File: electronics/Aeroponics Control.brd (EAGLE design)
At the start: 61.9 x 71.1 mm, 27 parts, among them IC1 7407N, K1 SRM-1C-SL-5VDC, Q1 FQP30N06L, Q2 FQP30N06L, Q6 FDU3N40TU

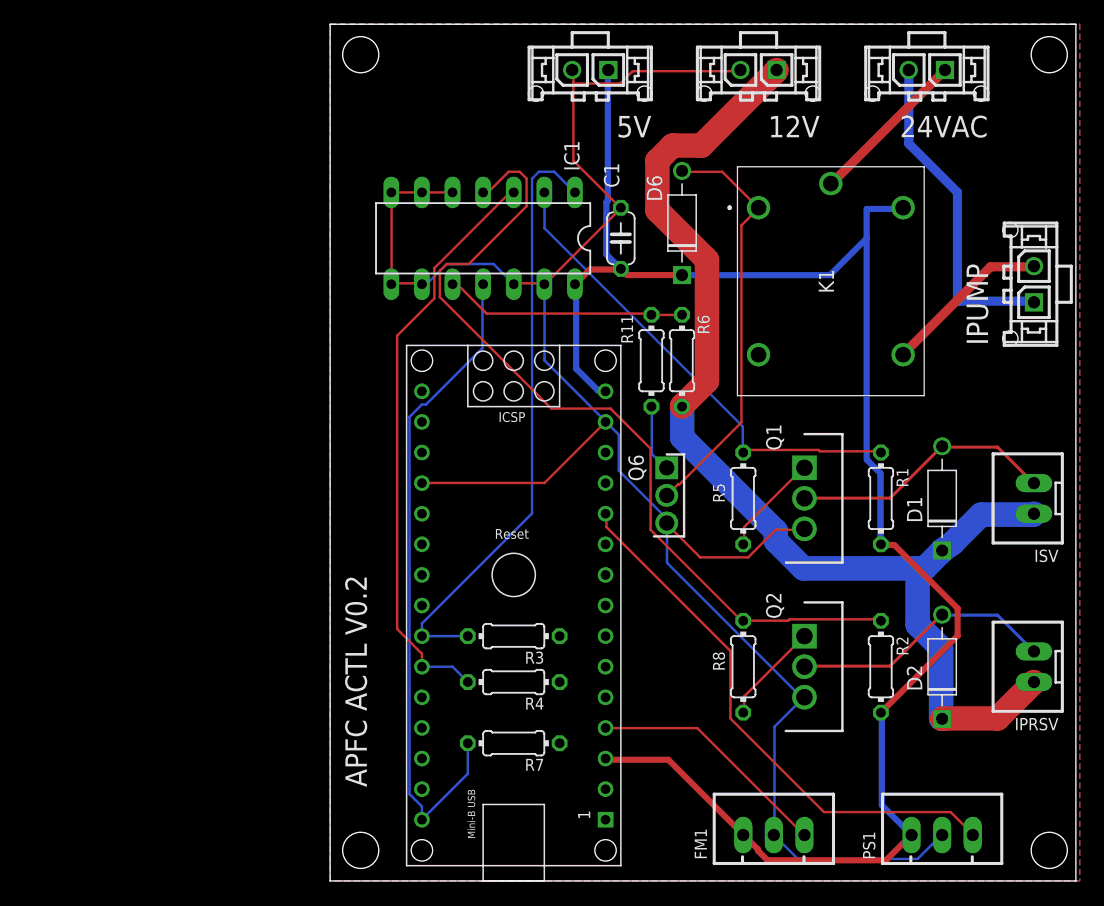
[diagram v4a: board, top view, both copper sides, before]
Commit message: Fixed FMS1 pin assignment on Nano. Incorpated fixed Relay library component.
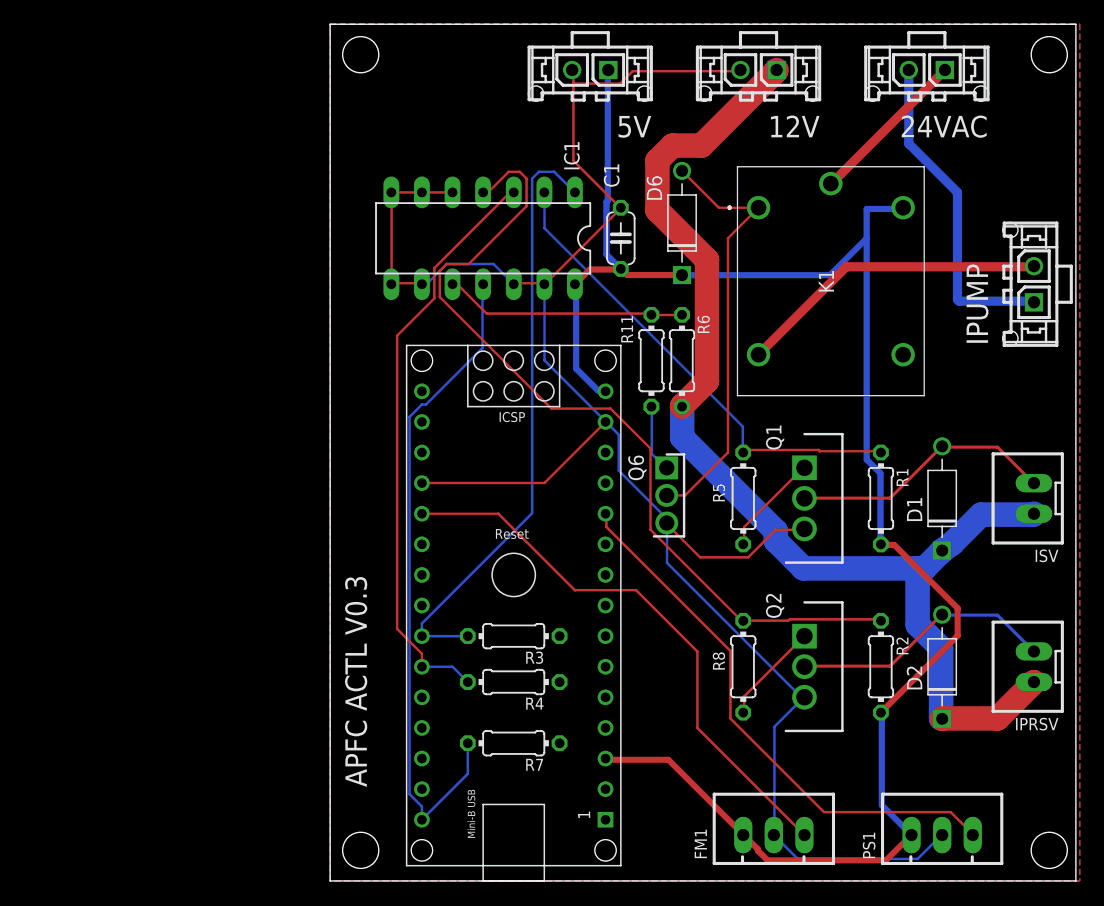
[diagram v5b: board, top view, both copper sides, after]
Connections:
- net FM1S: now also PCB1.20; no longer PCB1.4
- net N$7: now also K1.2; no longer K1.3
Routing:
- net FM1S: track 20.2 -> 46.5 mm
- net N$7: track 13.9 -> 25.9 mm
- net N$21: track 34.7 -> 35.5 mm
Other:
- board text added: "APFC ACTL V0.3"
- board text removed: "APFC ACTL V0.2"
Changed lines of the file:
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@@
 <hole x="97.79" y="2.54" drill="2.99999375"/>
 <hole x="40.64" y="2.54" drill="2.99999375"/>
-<text x="39.37" y="25.4" size="1.778" layer="25" rot="R270">APFC ACTL V0.2</text>
+<text x="39.37" y="25.4" size="1.778" layer="25" rot="R270">APFC ACTL V0.3</text>
 <text x="92.71" y="44.45" size="1.778" layer="25" rot="R90">IPUMP</text>
 <text x="92.71" y="63.5" size="1.778" layer="25" rot="R180">24VAC</text>
@@
 <signal name="FM1S">
 <contactref element="FM1" pad="3"/>
-<contactref element="PCB1" pad="4"/>
-<wire x1="68.58" y1="12.6873" x2="61.0362" y2="12.6873" width="0.2032" layer="1"/>
-<wire x1="77.3811" y1="3.8862" x2="68.58" y2="12.6873" width="0.2032" layer="1"/>
-<wire x1="61.0362" y1="12.6873" x2="60.96" y2="12.7" width="0.2032" layer="1"/>
-<wire x1="77.3811" y1="3.8862" x2="77.47" y2="3.81" width="0.2032" layer="1"/>
+<contactref element="PCB1" pad="20"/>
+<wire x1="45.72" y1="30.48" x2="52.07" y2="30.48" width="0.2032" layer="1"/>
+<wire x1="52.07" y1="30.48" x2="58.42" y2="24.13" width="0.2032" layer="1"/>
+<wire x1="58.42" y1="24.13" x2="63.5" y2="24.13" width="0.2032" layer="1"/>
+<wire x1="63.5" y1="24.13" x2="68.58" y2="19.05" width="0.2032" layer="1"/>
+<wire x1="68.58" y1="19.05" x2="68.58" y2="12.7" width="0.2032" layer="1"/>
+<wire x1="68.58" y1="12.7" x2="77.47" y2="3.81" width="0.2032" layer="1"/>
 </signal>
 <signal name="PS1S">
@@
 <contactref element="K1" pad="1"/>
 <contactref element="D6" pad="A"/>
-<wire x1="70.6374" y1="58.8645" x2="67.3227" y2="58.8645" width="0.2032" layer="1"/>
-<wire x1="73.6092" y1="55.8927" x2="70.6374" y2="58.8645" width="0.2032" layer="1"/>
-<wire x1="67.3227" y1="58.8645" x2="67.31" y2="58.935" width="0.2032" layer="1"/>
-<wire x1="73.6092" y1="55.8927" x2="73.66" y2="55.88" width="0.2032" layer="1"/>
-<wire x1="66.9798" y1="32.9184" x2="66.0654" y2="32.004" width="0.2032" layer="1"/>
-<wire x1="67.0941" y1="32.9184" x2="66.9798" y2="32.9184" width="0.2032" layer="1"/>
-<wire x1="72.2376" y1="38.0619" x2="67.0941" y2="32.9184" width="0.2032" layer="1"/>
-<wire x1="72.2376" y1="54.4068" x2="72.2376" y2="38.0619" width="0.2032" layer="1"/>
-<wire x1="73.6092" y1="55.7784" x2="72.2376" y2="54.4068" width="0.2032" layer="1"/>
-<wire x1="66.0654" y1="32.004" x2="66.04" y2="32" width="0.2032" layer="1"/>
-<wire x1="73.6092" y1="55.7784" x2="73.66" y2="55.88" width="0.2032" layer="1"/>
+<wire x1="66.04" y1="32" x2="67.56" y2="32" width="0.2032" layer="1"/>
+<wire x1="71.12" y1="53.34" x2="73.66" y2="55.88" width="0.2032" layer="1"/>
+<wire x1="67.56" y1="32" x2="71.12" y2="35.56" width="0.2032" layer="1"/>
+<wire x1="71.12" y1="35.56" x2="71.12" y2="53.34" width="0.2032" layer="1"/>
+<wire x1="73.66" y1="55.88" x2="70.365" y2="55.88" width="0.2032" layer="1"/>
+<wire x1="70.365" y1="55.88" x2="67.31" y2="58.935" width="0.2032" layer="1"/>
 </signal>
 <signal name="IPCTL">
@@
 </signal>
 <signal name="N$7" class="2">
-<contactref element="K1" pad="3"/>
+<contactref element="K1" pad="2"/>
 <contactref element="IPUMP" pad="P$2"/>
-<wire x1="92.9259" y1="50.9778" x2="96.4692" y2="50.9778" width="0.762" layer="1"/>
-<wire x1="85.725" y1="43.7769" x2="92.9259" y2="50.9778" width="0.762" layer="1"/>
 <wire x1="96.4692" y1="50.9778" x2="96.52" y2="51.03" width="0.762" layer="1"/>
-<wire x1="85.725" y1="43.7769" x2="85.66" y2="43.68" width="0.762" layer="1"/>
+<wire x1="73.66" y1="43.68" x2="80.9578" y2="50.9778" width="0.762" layer="1"/>
+<wire x1="80.9578" y1="50.9778" x2="96.4692" y2="50.9778" width="0.762" layer="1"/>
 </signal>
 <signal name="5V">
